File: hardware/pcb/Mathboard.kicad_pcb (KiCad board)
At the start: 4 copper layers, 95.6 x 73.6 mm, 90 parts, among them J3 TYPE-C sinking plate, Q1 2N7002VC-, Q2 2N7002VC-, SW1 SW_Push, SW10 SW_Push, SW11 SW_Push, SW12 SW_Push, SW13 SW_Push, SW14 SW_Push, SW15 SW_Push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

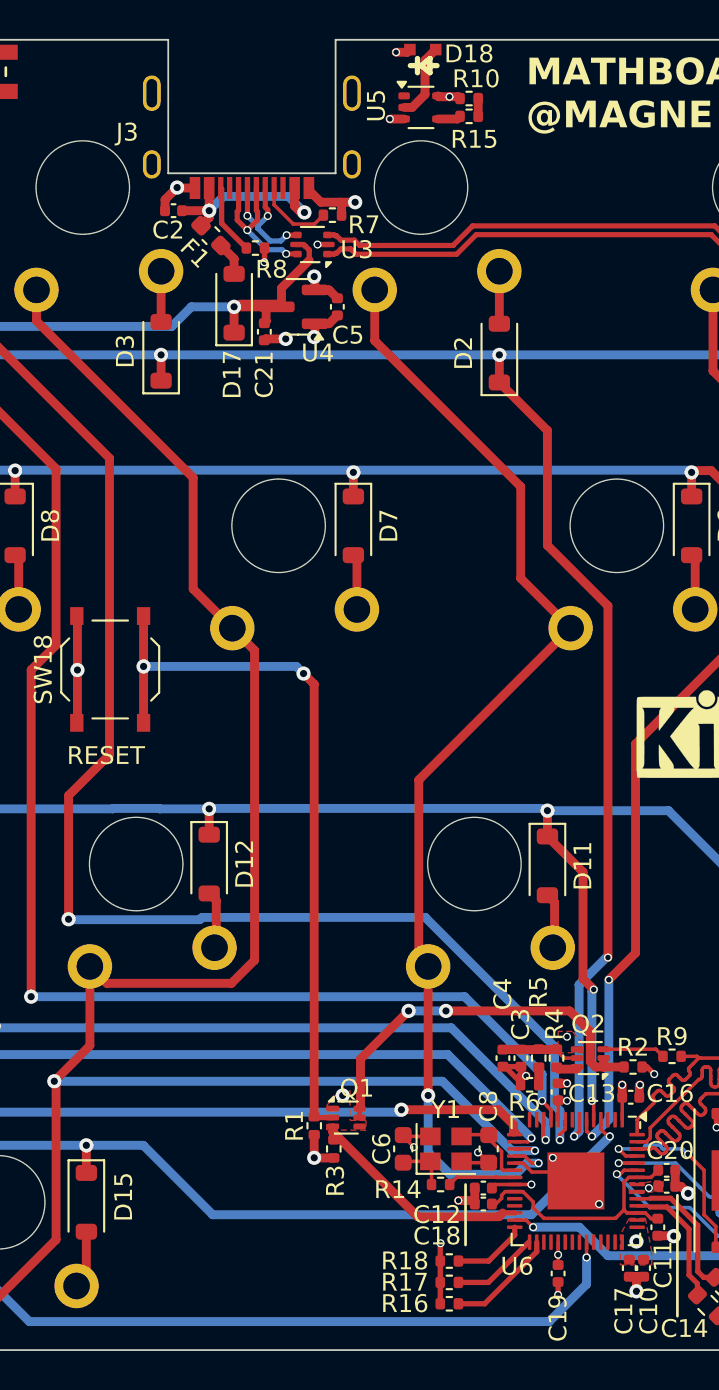
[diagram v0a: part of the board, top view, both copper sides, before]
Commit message: USB port fixed
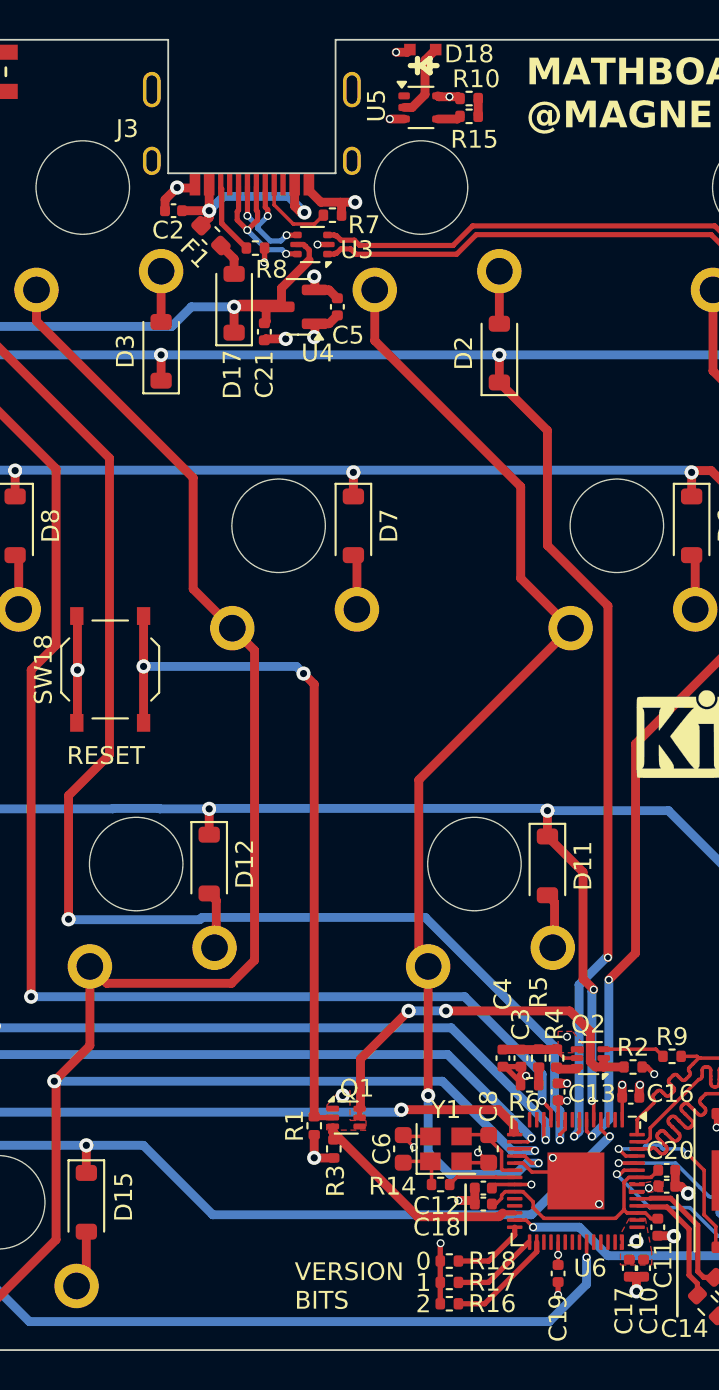
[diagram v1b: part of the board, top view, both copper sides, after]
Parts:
- moved J3 0.20 mm to (139.8, 46.8)
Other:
- board text added: "0"
- board text added: "1"
- board text added: "2"
- board text added: "VERSION BITS"
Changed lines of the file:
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@@
 		(tags "resistor")
 		(property "Reference" "R17"
-			(at 2.5 0 0)
+			(at -2.41 0 0)
 			(layer "F.SilkS")
 			(effects
@@
 		(tags "resistor")
 		(property "Reference" "R8"
-			(at -0.9 -1.2 360)
+			(at -0.9 -1.2 0)
 			(layer "F.SilkS")
 			(effects
@@
 		)
 		(property "Value" "5.1k"
-			(at 2.65 0.3 360)
+			(at 2.65 0.3 0)
 			(layer "F.Fab")
 			(effects
@@
 		)
 		(fp_text user "${REFERENCE}"
-			(at 0 0 360)
+			(at 0 0 0)
 			(layer "F.Fab")
 			(effects
@@
 	(footprint "mathboard:USB_C_Receptacle_XYECONN TYPE-C-F02C-1BBWC1.6"
 		(layer "F.Cu")
-		(at 139.8 47 180)
+		(at 139.8 46.8 180)
 		(descr "USB Type C, right-angle, SMT, https://datasheet.lcsc.com/lcsc/2204071530_G-Switch-GT-USB-7010ASV_C2988369.pdf")
 		(tags "USB C Type-C Receptacle SMD")
@@
 		(model "${KIPRJMOD}/resources/3d_models/USB - C inboard.STEP"
 			(offset
-				(xyz -0.977 11.05 -5.9)
+				(xyz -0.977 11.05 -5.8)
 			)
 			(scale
@@
 		(tags "resistor")
 		(property "Reference" "R14"
-			(at -2.4 0.3 0)
+			(at -2.7 0.1 0)
 			(layer "F.SilkS")
 			(effects
@@
 		(tags "capacitor")
 		(property "Reference" "C18"
-			(at 2.6 -1.8 0)
+			(at 2.6 -1.3 0)
 			(layer "F.SilkS")
 			(effects
@@
 		(tags "capacitor")
 		(property "Reference" "C2"
-			(at -0.3 1.1 360)
+			(at -0.3 1.1 0)
 			(layer "F.SilkS")
 			(effects
@@
 		)
 		(property "Value" "4.7u"
-			(at 0 1.16 360)
+			(at 0 1.16 0)
 			(layer "F.Fab")
 			(effects
@@
 		)
 		(fp_text user "${REFERENCE}"
-			(at 0 0 360)
+			(at 0 0 0)
 			(layer "F.Fab")
 			(effects
@@
 		(tags "resistor")
 		(property "Reference" "R16"
-			(at 2.5 0 0)
+			(at -2.41 0 0)
 			(layer "F.SilkS")
 			(effects
@@
 		(tags "QFN NoLead")
 		(property "Reference" "U6"
-			(at 4.8 3.3 0)
+			(at 4.9 -0.8 0)
 			(layer "F.SilkS")
 			(effects
@@
 		(tags "capacitor")
 		(property "Reference" "C12"
-			(at 2.6 -1.5 0)
+			(at 2.6 -1 0)
 			(layer "F.SilkS")
 			(effects
@@
 		(tags "resistor")
 		(property "Reference" "R18"
-			(at 2.5 0 0)
+			(at -2.41 0 0)
 			(layer "F.SilkS")
 			(effects
@@
 	)
 	(gr_line
-		(start 151.8 110.4)
+		(start 151.8 109.8)
 		(end 151.8 107)
 		(stroke
@@
 		)
 	)
+	(gr_text "2"
+		(at 149 114.3 0)
+		(layer "F.SilkS")
+		(effects
+			(font
+				(size 1 1)
+				(thickness 0.15)
+			)
+			(justify left bottom)
+		)
+	)
 	(gr_text "RESET"
 		(at 129.4 83.5 0)
@@
 		)
 	)
+	(gr_text "0"
+		(at 149 111.9 0)
+		(layer "F.SilkS")
+		(effects
+			(font
+				(size 1 1)
+				(thickness 0.15)
+			)
+			(justify left bottom)
+		)
+	)
+	(gr_text "1"
+		(at 149 113.1 0)
+		(layer "F.SilkS")
+		(effects
+			(font
+				(size 1 1)
+				(thickness 0.15)
+			)
+			(justify left bottom)
+		)
+	)
 	(gr_text "MATHBOARD V1.5\n@MAGNE LAURITZEN"
 		(at 155.2 47.8 0)
@@
 			)
 			(justify left bottom)
+		)
+	)
+	(gr_text "VERSION\nBITS"
+		(at 142.2 114.1 0)
+		(layer "F.SilkS")
+		(effects
+			(font
+				(size 1 1)
+				(thickness 0.15)
+			)
+			(justify left bottom)

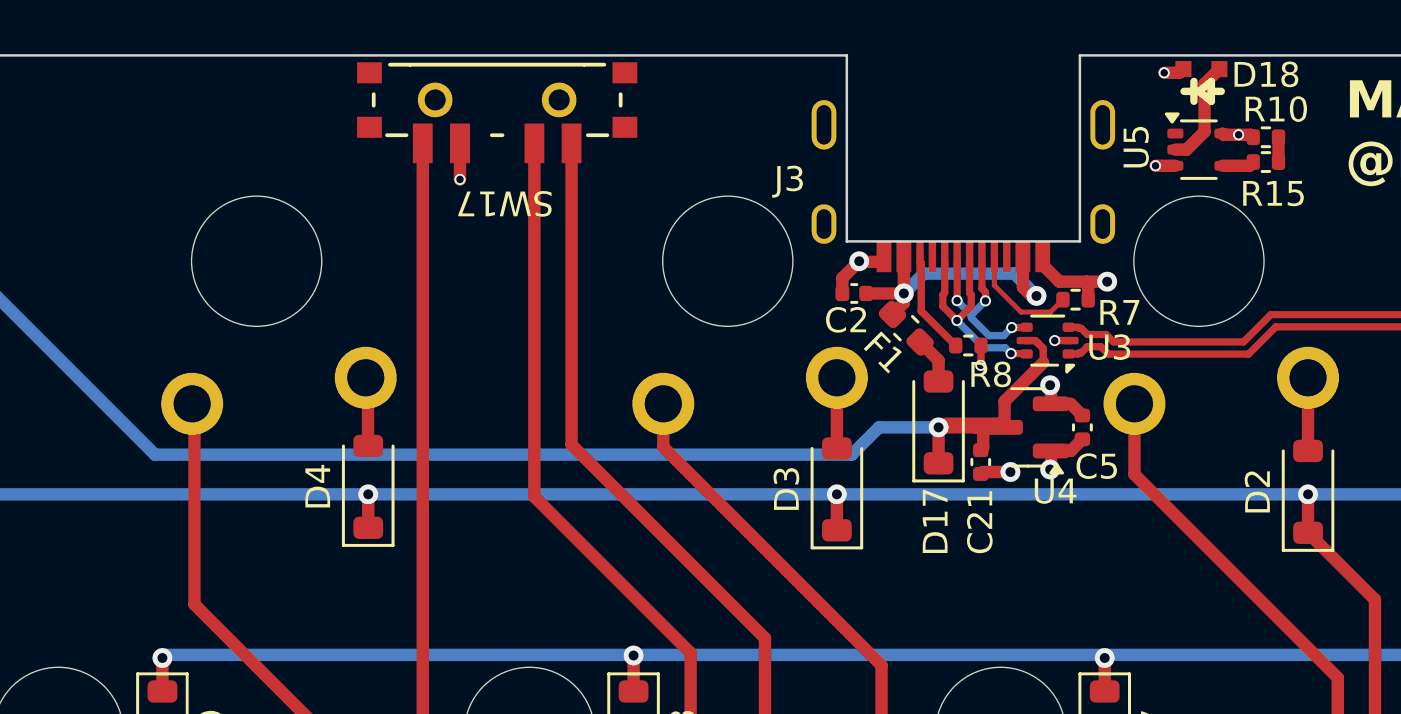
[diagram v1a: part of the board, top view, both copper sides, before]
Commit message: V1.5 gerbers and changes to the USB layout
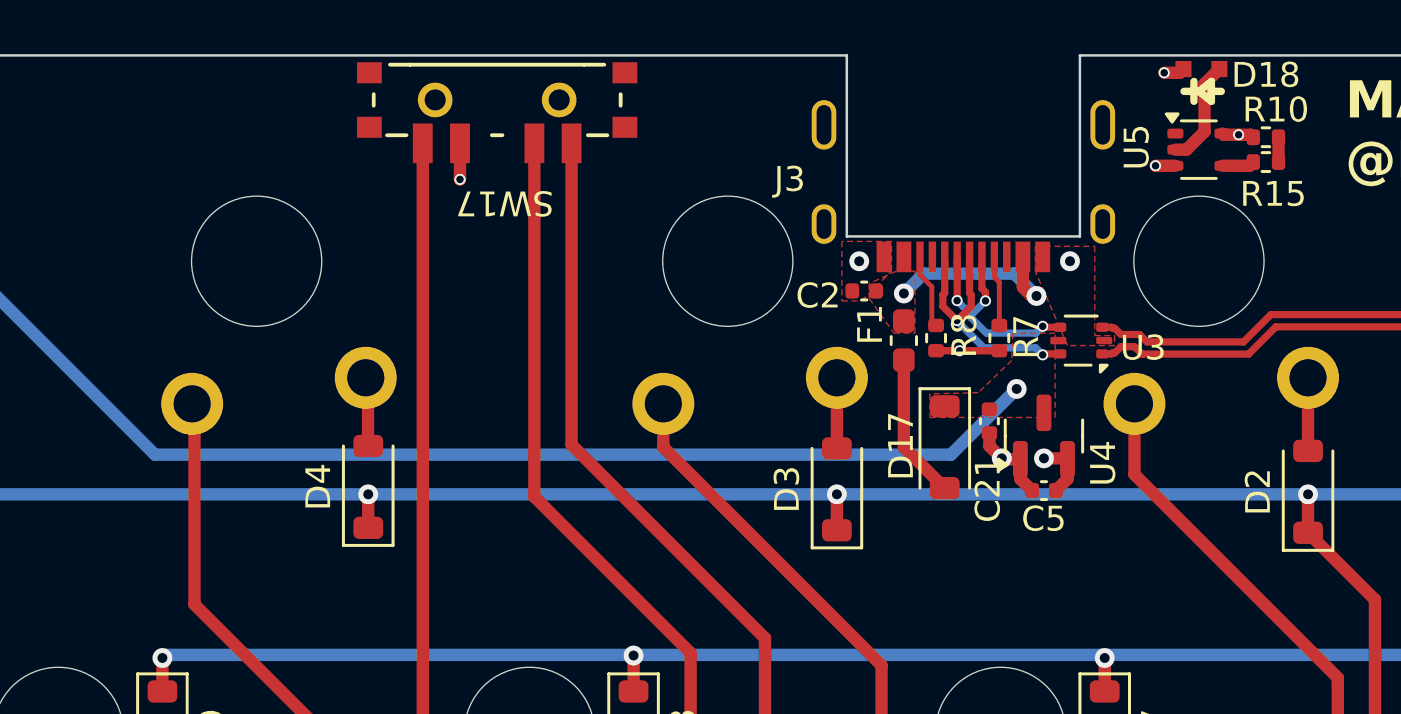
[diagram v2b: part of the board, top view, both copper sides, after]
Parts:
- moved R7 3.44 mm to (141.2, 54.1), turned to 90 degrees
- moved C5 2.98 mm to (143.1, 60.2), turned to 180 degrees
- moved C21 1.69 mm to (140.8, 57.5)
- moved U3 1.35 mm to (144.6, 54.2)
- moved R8 1.33 mm to (138.7, 54.1), turned to 90 degrees
- moved D17 1.03 mm to (139.1, 58.5), turned to -90 degrees
- moved U4 0.74 mm to (143.1, 58.0), turned to 90 degrees
- moved F1 0.51 mm to (137.4, 54.2), turned to -90 degrees
- moved C2 0.41 mm to (135.8, 52.2)
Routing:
- net +5V: track 80.6 -> 72.0 mm
- net GND: track 49.4 -> 44.3 mm, vias 32 -> 30
- net Net-(D17-A): track 1.90 -> 5.85 mm
- net VBUS: track 11.6 -> 7.85 mm
- net Net-(J3-CC1): track 4.24 -> 2.85 mm
- net /Microcontroller/PORT+: track 8.79 -> 10.2 mm
- net /Microcontroller/USB-: track 94.4 -> 93.1 mm
- net /Microcontroller/USB+: track 94.3 -> 92.9 mm
- net Net-(J3-CC2): track 4.37 -> 3.03 mm
- net /Microcontroller/PORT-: track 7.67 -> 8.97 mm
- added copper zone on F.Cu, net +5V
- added copper zone on F.Cu, net VBUS
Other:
- outline, holes or cut-outs redrawn
